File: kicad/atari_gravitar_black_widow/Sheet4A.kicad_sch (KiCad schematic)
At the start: 0 parts

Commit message: 4A DONE
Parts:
- added R19: 1k, quantum_arcade_pcb:GenComp, symbol Device:R
- added U?: LS138, symbol quantum_arcade_pcb:LS138
- added U? (x2): LS04, symbol atari_grav_bw:LS04
- added U?: LS245, symbol atari_grav_bw:LS245
- added U?: LS10, symbol atari_grav_bw:LS10
- added U?: 6502, symbol atari_grav_bw:6502
- added U? (x2): LS00, symbol Asteroids:LS00
- added U?: LS244C, symbol atari_grav_bw:LS244C
- added U?: LS04, symbol Asteroids:LS04
- added U?: LS161, symbol Asteroids:LS161
- added U? (x2): 136010-X, symbol atari_grav_bw:136010-X
- added U?: LS244A, symbol atari_grav_bw:LS244A
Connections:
- new net: U?.19 (CE), U?.3
- new net: U?.10 (AB1), U?.4 (I1a)
- new net: U?.11 (AB2), U?.6 (I2a)
- new net: U?.12 (AB3), U?.8 (I3a)
- new net: U?.13 (AB4), U?.17 (I3b)
- new net: U?.14 (AB5), U?.15 (I2b)
- new net: U?.13 (I1b), U?.15 (AB6)
- new net: U?.11 (I0b), U?.16 (AB7)
- new net: U?.17 (AB8), U?.4 (I1a)
- new net: U?.18 (AB9), U?.6 (I2a)
- new net: R19.1, U?.2 (RDY), U?.38 (SO), U?.6 (NMI_)
- new net: U?.13 (I1b), U?.20 (AB11)
- new net: U?.15 (I2b), U?.22 (AB12)
- new net: U?.10 (ET), U?.11, U?.4 (IRQ_)
- new net: U?.2 (I0a), U?.9 (AB0)
- new net: U?.12 (QC), U?.13
- new net +5V: R19.2, U?.16 (VCC), U?.16 (VCC), U?.16 (VCC)
- new net 1.5MHZ: U?.2 (I0a), U?.37 (O0(IN))
- new net 3KHZ: U?.1 (C)
- new net 3MHZ: U?.3
- new net A10: U?.19 (AB10), U?.8 (I3a)
- new net A13: U?.12 (A2), U?.12 (A2), U?.23 (AB13), U?.9
- new net A14: U?.13 (A3), U?.13 (A3), U?.24 (AB14)
- new net A15: U?.14 (A4), U?.14 (A4), U?.25 (AB15)
- new net AB0: U?.18 (O0a)
- new net AB1: U?.16 (O1a)
- new net AB10: U?.12 (O3a)
- new net AB11: U?.10 (A0), U?.10 (A0), U?.7 (O1b)
- new net AB12: U?.11 (A1), U?.11 (A1), U?.5 (O2b)
- new net AB2: U?.14 (O2a)
- new net AB3: U?.12 (O3a)
- new net AB4: U?.3 (O3b)
- new net AB5: U?.5 (O2b)
- new net AB6: U?.1 (A), U?.7 (O1b)
- new net AB7: U?.2 (B), U?.9 (O0b)
- new net AB8: U?.16 (O1a), U?.3 (C)
- new net AB9: U?.14 (O2a)
- new net BPHI2: U?.13, U?.5, U?.9 (O0b)
- new net D0: U?.18 (B0), U?.33 (DB0)
- new net D1: U?.17 (B1), U?.32 (DB1)
- new net D2: U?.16 (B2), U?.31 (DB2)
- new net D3: U?.15 (B3), U?.30 (DB3)
- new net D4: U?.14 (B4), U?.29 (DB4)
- new net D5: U?.13 (B5), U?.28 (DB5)
- new net D6: U?.12 (B6), U?.27 (DB6)
- new net D7: U?.11 (B7), U?.26 (DB7)
- new net DB0: U?.2 (A0)
- new net DB1: U?.3 (A1)
- new net DB2: U?.4 (A2)
- new net DB3: U?.5 (A3)
- new net DB4: U?.6 (A4)
- new net DB5: U?.7 (A5)
- new net DB6: U?.8 (A6)
- new net DB7: U?.9 (A7)
- new net GND: U?.1 (VSS), U?.15 (E), U?.21 (VSS), U?.8 (GND), U?.8 (GND), U?.8 (GND)
- new net LATCH: U?.15 (Y0)
- new net PHI 2: U?.11 (I0b), U?.39 (O2(OUT))
- new net PR23: U?.7 (EP), U?.9 (LD)
- new net ROM: U?.1, U?.1 (B0), U?.9 (B7)
- new net R/~{W}: U?.17 (I3b), U?.34 (R/~{W})
- new net R/~{W}B: U?.1, U?.3 (O3b)
- new net VGCK: U?.18 (O0a)
- new net ~{AB13}: U?.8
- new net ~{BPHI2}: U?.12
- new net ~{EAROMCON}: U?.11 (Y4)
- new net ~{EAROMRD}: U?.5 (B4)
- new net ~{EAROMWR}: U?.10 (Y5)
- new net ~{INTACT}: U?.12 (Y3), U?.2 (CLK)
- new net ~{IO}: U?.4 (~{G2A}), U?.9 (B7)
- new net ~{I/O1}: U?.2 (B2)
- new net ~{I/O5}: U?.2, U?.3 (B1)
- new net ~{I/OO}: U?.1 (B0)
- new net ~{RAM}: U?.9 (B7)
- new net ~{RESET}: U?.40 (RES_)
- new net ~{ROM0}: U?.2 (B2)
- new net ~{ROM1}: U?.3 (B1)
- new net ~{ROM2}: U?.5 (B4)
- new net ~{ROM3}: U?.6 (B5)
- new net ~{ROM4}: U?.7 (B6)
- new net ~{ROM5}: U?.9 (B7)
- new net ~{R}/WB: U?.2, U?.4
- new net ~{SINP1}: U?.6 (B5)
- new net ~{SINP2}: U?.7 (B6)
- new net ~{VGGO}: U?.14 (Y1)
- new net ~{VGRST}: U?.13 (Y2)
- new net ~{WDCLR}: U?.9 (Y6)
- new net ~{WRITE}: U?.5 (~{G2B}), U?.6
- no-connect marks 0 -> 7
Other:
- note added: "ADDRESS DECODER"
- note added: "MIROPROCESSOR"

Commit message: REVIEW 4A DONE
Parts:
- F_3: renamed from U?; value LS04 -> S04
- K_4: renamed from U?; value LS10 -> S10
- R_1: renamed from U?; value 136010-X -> 136010-X11
- R_2: renamed from U?; value 136010-X -> 136010-X12
- gave numbers to parts that had none: 9
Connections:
- net ~{I/OO} is gone; now on net ~{RAM}: R_2.1 (B0)
- net +5V: now also B_1.20 (VCC), C_1.20 (VCC), C_2.8 (VCC), F_2.20 (VCC), F_3.14 (VCC), R_4.14 (VCC)
- net 3KHZ: now also J_4.2 (CLK); no longer J_4.1 (C)
- net GND: now also B_1.1 (OEa), B_1.10 (GND), B_1.19 (OEb), C_1.1 (OEa), C_1.10 (GND), C_1.19 (OEb), F_2.10 (GND), F_3.7 (GND), J_4.3 (A), J_4.4 (B), J_4.5 (C), J_4.6 (D), J_4.8 (GND), R_2.15 (E), R_4.7 (GND)
- net PR23: now also P_3.6 (G1)
- net ROM: now also R_1.2 (B2); no longer R_1.9 (B7)
- net R/~{W}B: now also F_2.1 (DIR)
- net ~{INTACT}: now also J_4.1 (C); no longer J_4.2 (CLK)
- net ~{I/O1}: now also R_2.3 (B1); no longer R_2.2 (B2)
- net ~{I/O5}: now also R_2.4 (B3); no longer R_2.3 (B1)
- net ~{RAM}: no longer R_2.9 (B7)
- net ~{ROM0}: now also R_1.3 (B1); no longer R_1.2 (B2)
- net ~{ROM1}: now also R_1.4 (B3); no longer R_1.3 (B1)
- net at L_3.12: now also J_4.11 (QD)
- new net ~{I/O0}: R_2.2 (B2)
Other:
- moved on the sheet: C_2

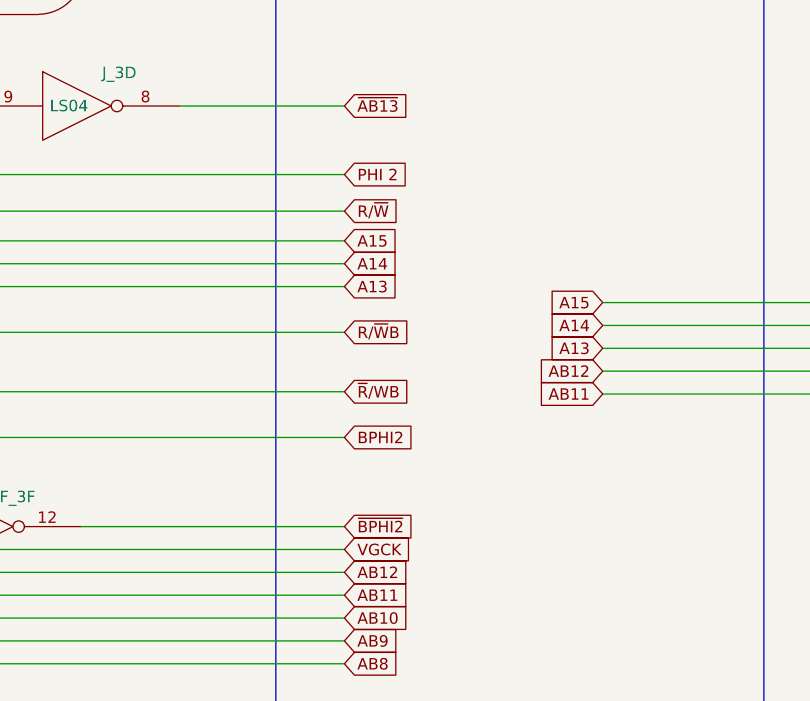
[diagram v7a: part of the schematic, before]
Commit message: Sheets 5A and 5B
Also subbed Φ for PHI in Φ2, BΦ2 and ~{BΦ2}
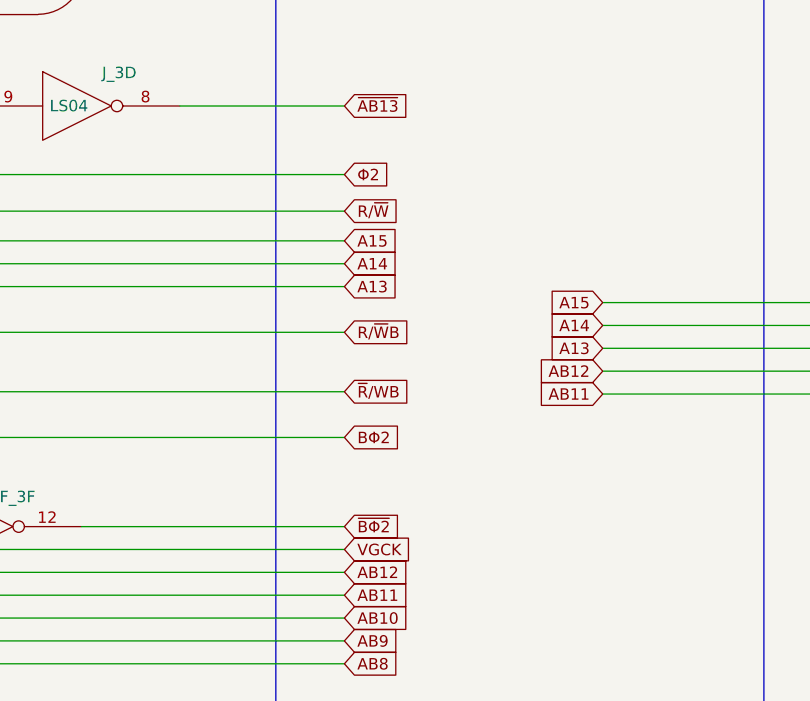
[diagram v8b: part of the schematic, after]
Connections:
- net BPHI2 renamed BΦ2
- net PHI 2 renamed Φ2
- net ~{BPHI2} renamed ~{BΦ2}
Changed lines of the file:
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@@
     )
   )
-  (global_label "PHI 2" (shape input) (at 319.786 67.564 0) (fields_autoplaced)
-    (effects (font (size 1.27 1.27)) (justify left))
-    (property "Intersheet References" "${INTERSHEET_REFS}" (id 0) (at 327.4926 67.4846 0)
+  (global_label "Φ2" (shape input) (at 319.786 67.564 0) (fields_autoplaced)
+    (effects (font (size 1.27 1.27)) (justify left))
+    (property "Intersheet References" "${INTERSHEET_REFS}" (id 0) (at 324.6502 67.4846 0)
       (effects (font (size 1.27 1.27)) (justify left) hide)
     )
@@
     )
   )
-  (global_label "BPHI2" (shape input) (at 319.786 96.774 0) (fields_autoplaced)
-    (effects (font (size 1.27 1.27)) (justify left))
-    (property "Intersheet References" "${INTERSHEET_REFS}" (id 0) (at 327.795 96.6946 0)
-      (effects (font (size 1.27 1.27)) (justify left) hide)
-    )
-  )
-  (global_label "~{BPHI2}" (shape input) (at 319.786 106.68 0) (fields_autoplaced)
-    (effects (font (size 1.27 1.27)) (justify left))
-    (property "Intersheet References" "${INTERSHEET_REFS}" (id 0) (at 327.795 106.6006 0)
+  (global_label "BΦ2" (shape input) (at 319.786 96.774 0) (fields_autoplaced)
+    (effects (font (size 1.27 1.27)) (justify left))
+    (property "Intersheet References" "${INTERSHEET_REFS}" (id 0) (at 325.9202 96.6946 0)
+      (effects (font (size 1.27 1.27)) (justify left) hide)
+    )
+  )
+  (global_label "~{BΦ2}" (shape input) (at 319.786 106.68 0) (fields_autoplaced)
+    (effects (font (size 1.27 1.27)) (justify left))
+    (property "Intersheet References" "${INTERSHEET_REFS}" (id 0) (at 325.9202 106.6006 0)
       (effects (font (size 1.27 1.27)) (justify left) hide)
     )
@@
     (pin "2")
     (pin "3")
+    (pin "4")
     (pin "5")
     (pin "6")
     (pin "7")
     (pin "8")
-    (pin "4")
     (pin "9")
   )
@@
     (pin "2")
     (pin "3")
+    (pin "4")
     (pin "5")
     (pin "6")
     (pin "7")
     (pin "8")
-    (pin "4")
     (pin "9")
   )
